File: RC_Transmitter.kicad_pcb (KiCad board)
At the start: 2 copper layers, 153 x 100 mm, 17 parts, among them SW1 SW_SPDT_MSM, SW2 SW_SPDT_MSM

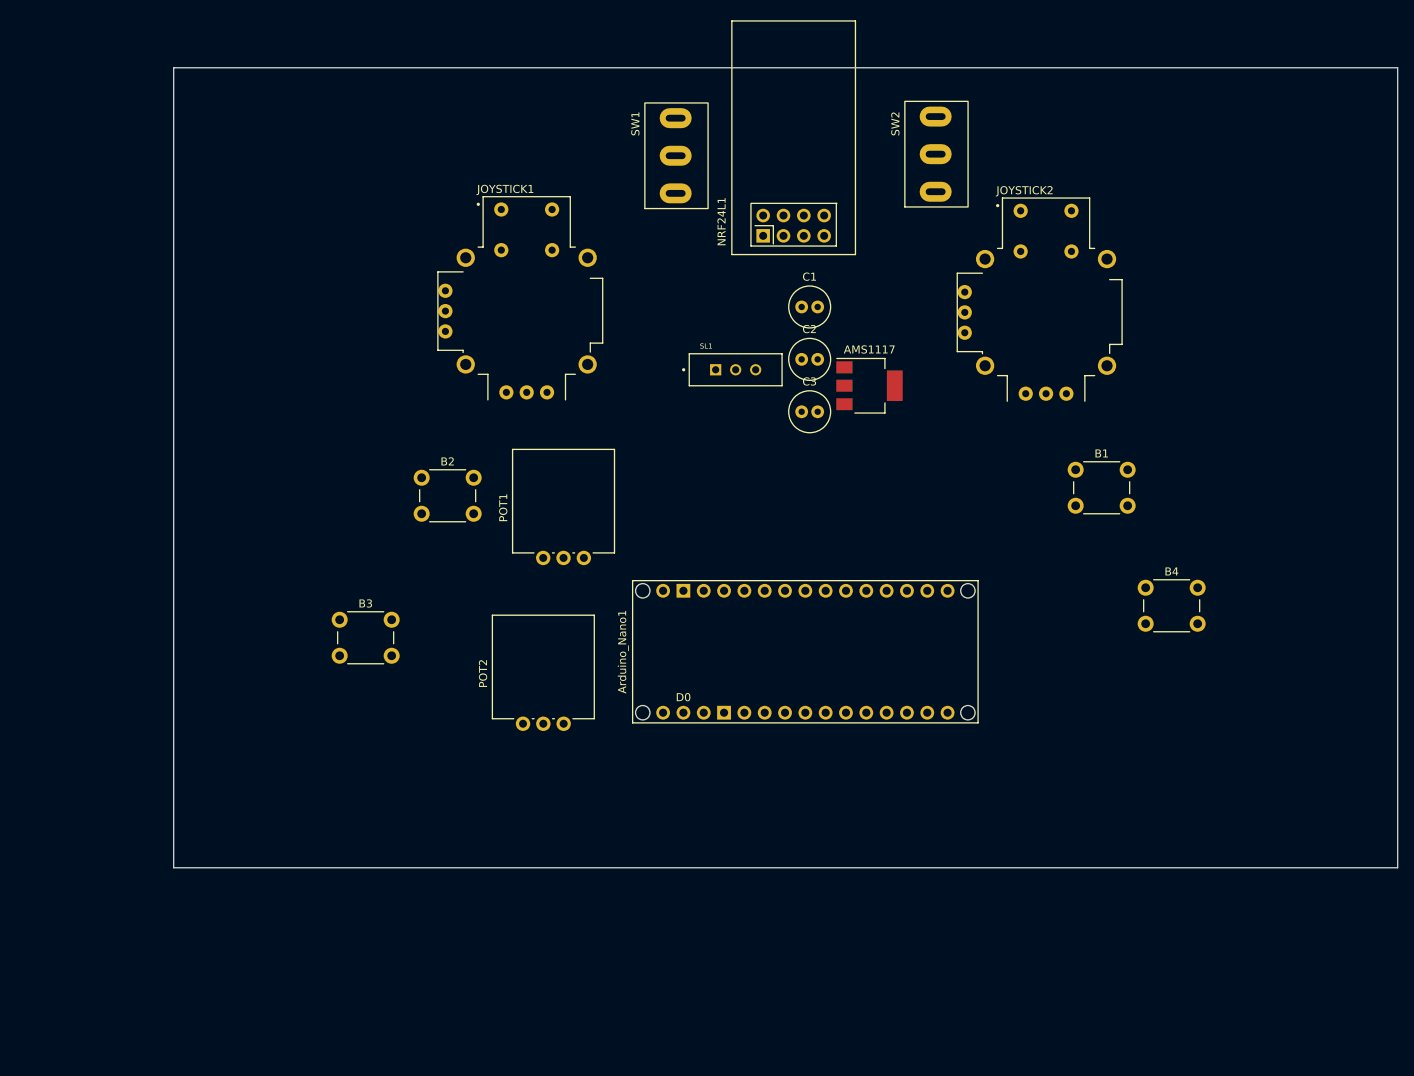
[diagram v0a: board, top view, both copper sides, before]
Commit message: Schematic Partial and PCB Init
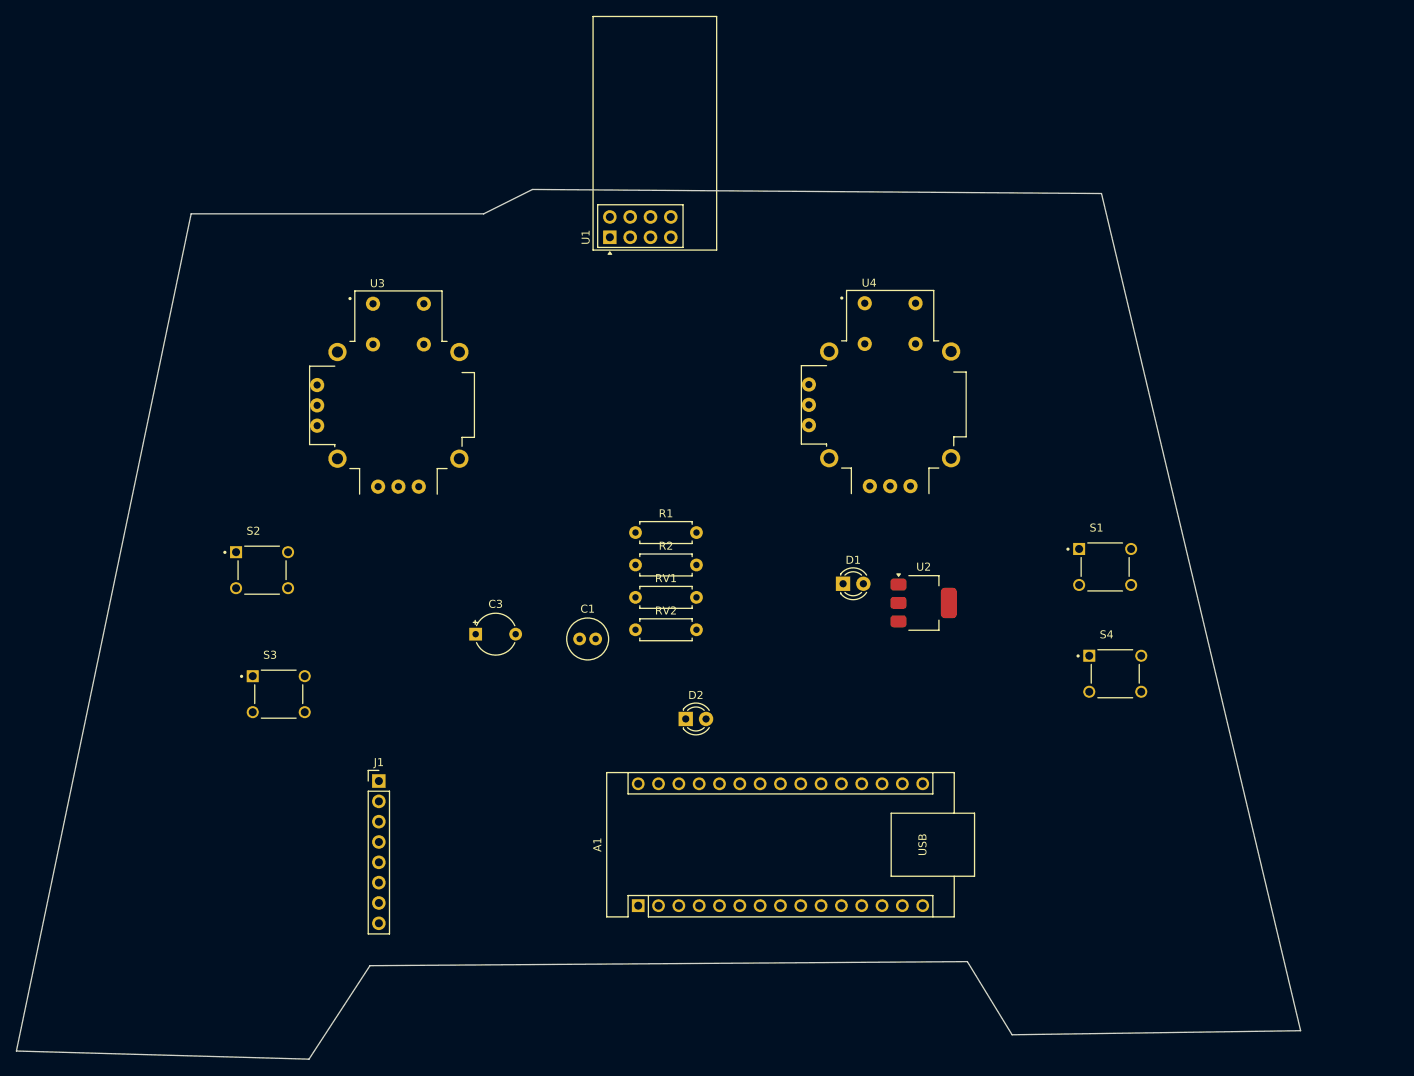
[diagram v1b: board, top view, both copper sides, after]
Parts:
- removed AMS1117: AMS1117-3.3, Package_TO_SOT_SMD:SOT-223-3_TabPin2
- removed Arduino_Nano1: Arduino_Nano_Socket, PCM_arduino-library:Arduino_Nano_Socket
- removed B1, B2, B3, B4: SW_Push_Dual, Button_Switch_THT:SW_PUSH_6mm_H4.3mm
- removed C2: 10uF, Capacitor_THT:C_Radial_D5.0mm_H11.0mm_P2.00mm
- removed JOYSTICK1, JOYSTICK2: COM-09032, COM_09032:XDCR_COM-09032
- removed NRF24L1: NRF24L01_Breakout, RF_Module:nRF24L01_Breakout
- removed POT1, POT2: Pot, Potentiometer_THT:Potentiometer_Vishay_248GJ-249GJ_Single_Vertical
- removed SL1: MINI-SPDT-SW, MINI-SPDT-SW:SW_MINI-SPDT-SW
- removed SW1, SW2: SW_SPDT_MSM, COM_09032:MTS-123
- added A1: Arduino_Nano_v3.x, Module:Arduino_Nano, F.Cu at (115.3, 134.7)
- added D1: LED, LED_THT:LED_D3.0mm_Clear, F.Cu at (140.9, 94.5)
- added D2: LED, LED_THT:LED_D3.0mm_Clear, F.Cu at (121.3, 111.4)
- added J1: MPU6050, Connector_PinHeader_2.54mm:PinHeader_1x08_P2.54mm_Vertical, F.Cu at (82.9, 119.2)
- added R1: 130, Resistor_THT:R_Axial_DIN0207_L6.3mm_D2.5mm_P7.62mm_Horizontal, F.Cu at (115.0, 88.1)
- added R2: 560, Resistor_THT:R_Axial_DIN0207_L6.3mm_D2.5mm_P7.62mm_Horizontal, F.Cu at (115.0, 92.2)
- added RV1: 10K, Resistor_THT:R_Axial_DIN0207_L6.3mm_D2.5mm_P7.62mm_Horizontal, F.Cu at (115.0, 96.2)
- added RV2: 10K, Resistor_THT:R_Axial_DIN0207_L6.3mm_D2.5mm_P7.62mm_Horizontal, F.Cu at (115.0, 100.2)
- added S1: TS02-66-60-BK-160-SCR-D, TS02-66-60-BK-160-SCR-D:SW_TS02-66-60-BK-160-SCR-D, F.Cu at (173.7, 92.4)
- added S2: TS02-66-60-BK-160-SCR-D, TS02-66-60-BK-160-SCR-D:SW_TS02-66-60-BK-160-SCR-D, F.Cu at (68.3, 92.8)
- added S3: TS02-66-60-BK-160-SCR-D, TS02-66-60-BK-160-SCR-D:SW_TS02-66-60-BK-160-SCR-D, F.Cu at (70.4, 108.3)
- added S4: TS02-66-60-BK-160-SCR-D, TS02-66-60-BK-160-SCR-D:SW_TS02-66-60-BK-160-SCR-D, F.Cu at (174.9, 105.8)
- added U1: NRF24L01_Breakout, RF_Module:nRF24L01_Breakout, F.Cu at (111.8, 51.2)
- added U2: AMS1117-3.3, Package_TO_SOT_SMD:SOT-223-3_TabPin2, F.Cu at (151.0, 96.9)
- added U3: COM-09032, COM_09032:XDCR_COM-09032, F.Cu at (85.3, 72.2)
- added U4: COM-09032, COM_09032:XDCR_COM-09032, F.Cu at (146.8, 72.1)
- C3: value 10uF -> 22uF; footprint Capacitor_THT:C_Radial_D5.0mm_H11.0mm_P2.00mm -> Capacitor_THT:CP_Radial_Tantal_D5.0mm_P5.00mm
- moved C1 49.9 mm to (108.0, 101.4)
- moved C3 49.3 mm to (95.0, 100.8)
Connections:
- C1 pad 1: +3.3V -> +3V_REGULATOR
- C3 pad 1: GND -> +3V_REGULATOR
- C3 pad 2: +3.3V -> GND
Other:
- board size 153 x 100 mm -> 160.5 x 108.7 mm
